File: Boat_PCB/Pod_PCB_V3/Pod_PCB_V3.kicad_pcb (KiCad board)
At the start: 2 copper layers, 48 x 63 mm, 54 parts, among them J1 Tether, J10 Aux, J2 pH SEN0161-V2, J3 TDS SEN0244 via DFR0504, J4 DO SEN0237-A (fit later), J5 Turbidity SEN0189, J6 Pressure SEN0257, J7 DS18B20, J8 Leak probe, J9 Bottom contact, U1 Pololu D36V6F5, U2 AP2112K-3.3, U3 XIAO ESP32-S3, U4 THVD2410, U5 ADS1115

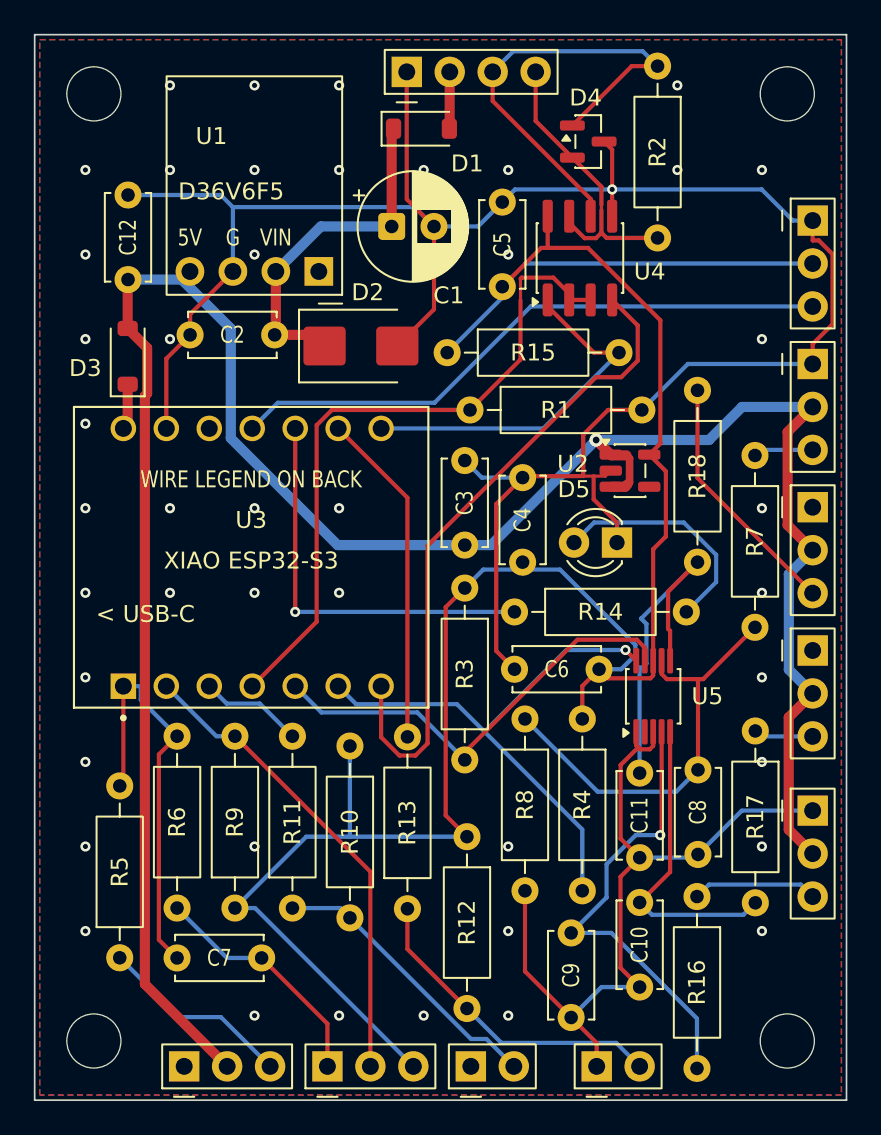
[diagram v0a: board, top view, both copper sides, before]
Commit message: feat(pcb): pod board rev B, reviewed and re-placed on a grid
Pod (Boat_PCB/Pod_PCB_V3), against rev A at 5b3b610. Same 54 footprints,
outline (48 x 63 mm) and netlist; the schematic is untouched.

- Review: every net checks out and every part is needed, so nothing was
  removed. The real faults were decoupling distances: the AP2112's caps
  C3/C4 sat 9.3/9.8 mm from its pins (now 2.2/2.7 mm), C5 was 5.0 mm
  from the THVD2410 (now 2.7) and C6 3.2 mm from the ADS1115 (now 2.3).
- Placement: the right-edge wire-pad groups are on one 8.47 mm pitch and
  the bottom groups on equal 3.4 mm gaps. The twelve upright resistors
  and caps stand in one row on a 3.4 mm pitch; the RX pull-up, DE
  pull-down and LED resistors form a column, and the PRESS/DO series
  resistors sit side by side.
- Back legend on a fixed grid: pad labels level with or centred on their
  pads, group names in one column (right edge) and one row (bottom
  edge), title block centred on the XIAO. Every pad is labelled; rev A
  had no GND label on TDS.
- Re-routed. Track length 1023 -> 949 mm. Vias 50 -> 46: nine GND
  stitching vias dropped and two moved off the legend rows, one TDS_OUT
  via moved 1.2 mm.
- The per-pad solid GND connection moved from C3 to U5 pad 3, the pad
  whose thermal spokes the new routing starves.

ERC 0 -> 0. DRC 0 -> 0. Schematic parity 0 -> 0. Unconnected 0 -> 0.

Docs: CLAUDE.md pod baseline and design brief section 5.

Co-Authored-By: Claude Opus 5.5 <noreply@anthropic.com>
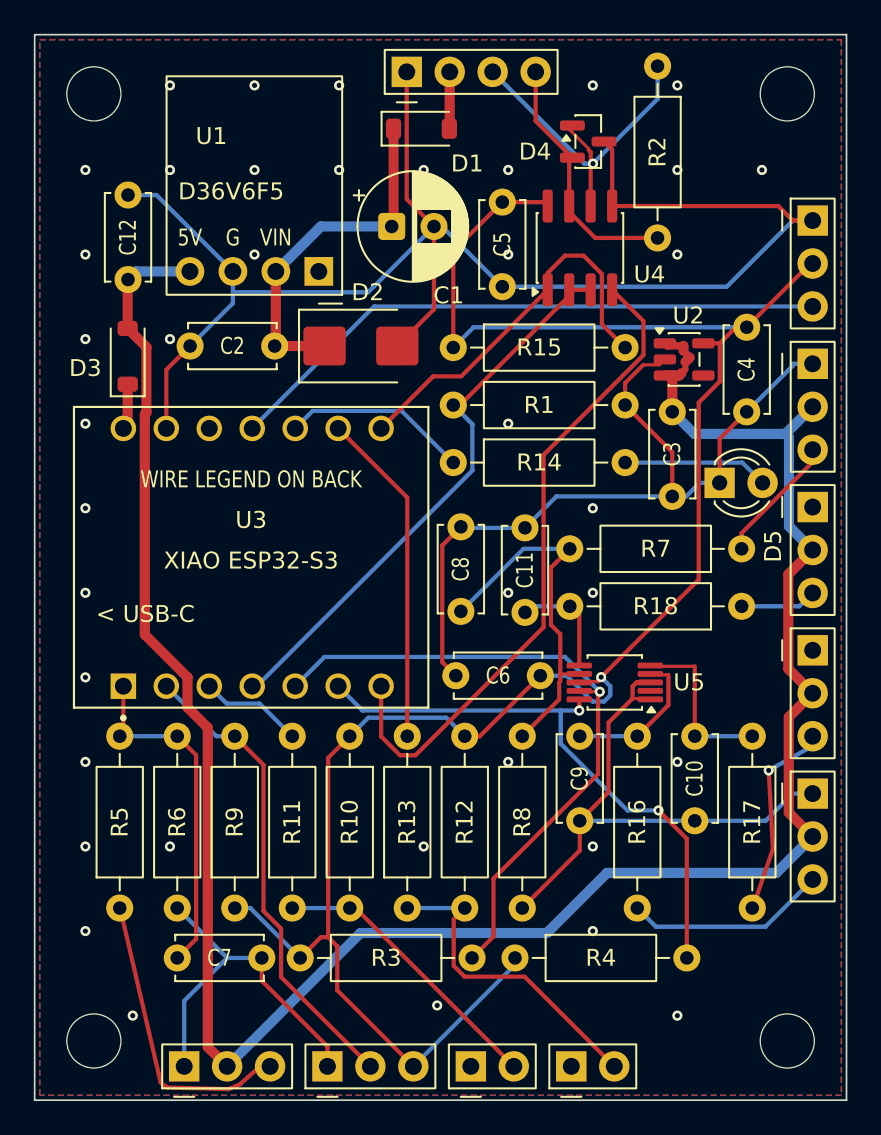
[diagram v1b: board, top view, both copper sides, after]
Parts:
- moved R3 23.9 mm to (115.7, 104.6), turned to 0 degrees
- moved C4 19.2 mm to (142.1, 67.3), turned to -90 degrees
- moved C8 16.9 mm to (125.2, 84.1), turned to 90 degrees
- moved R4 14.7 mm to (128.4, 104.6), turned to 0 degrees
- moved C3 14.6 mm to (137.7, 72.3), turned to -90 degrees
- moved R18 13.0 mm to (141.8, 83.8), turned to 180 degrees
- moved C11 11.7 mm to (129.0, 84.2), turned to 90 degrees
- moved C9 11.6 mm to (132.2, 91.5)
- moved R17 10.5 mm to (142.4, 101.6), turned to 90 degrees
- moved C10 10.4 mm to (139.0, 91.5)
- moved R14 9.54 mm to (124.8, 75.3)
- moved U2 7.32 mm to (138.4, 69.2)
- moved D5 7.02 mm to (140.5, 76.5), turned to 0 degrees
- moved R12 5.94 mm to (125.4, 91.5)
- moved R7 5.58 mm to (141.8, 80.4), turned to 180 degrees
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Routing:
- net /PH_AIN: track 27.4 -> 8.88 mm, vias 1 -> 0
- net /DO_AIN: track 20.8 -> 6.53 mm
- net /I2C_SDA: track 26.7 -> 39.6 mm, vias 0 -> 1
- net /LED_DRV: track 23.8 -> 11.0 mm, vias 1 -> 0
- net +3V3: track 133.8 -> 121.1 mm, vias 0 -> 1
- net /DO_OUT: track 14.8 -> 4.53 mm
- net /TDS_AIN: track 18.3 -> 10.2 mm
- net /TDS_OUT: track 3.52 -> 11.0 mm, vias 0 -> 1
- net /TETHER_A: track 28.0 -> 21.1 mm, vias 0 -> 1
- net /RS485_DE: track 40.4 -> 33.8 mm
- net /LED_A: track 13.8 -> 8.63 mm
- net /TURB_RAW: track 11.5 -> 16.7 mm
- net /PH_OUT: track 7.43 -> 12.0 mm
- net /TURB_ADC: track 24.9 -> 20.5 mm
- net /PRESS_RAW: track 3.55 -> 7.60 mm
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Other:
- board text added: "rev B 2026-09-29"
- board text removed: "rev A 2026-09-26"

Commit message: chore(pcb): V3 carrier and pod order-number markers for PCBWay
Like V3.1, the V3 carrier and the pod will be made by PCBWay, so their
back-silk order-number markers change from JLCPCB's "JLCJLCJLCJLC" to
PCBWay's "WayWayWay" (same spot, size and angle). Pick "Specify a
location" for the product number at checkout. Silkscreen only: the back
silkscreen gerber is the only one that changes on each board. CLAUDE.md
gets a short note on ordering.

Boat_PCB_V3 (rev E): 130.6 x 101.5 mm, 137 footprints, unchanged.
Pod_PCB_V3 (rev B): 48 x 63 mm, 54 footprints, unchanged.
Both: DRC 0 -> 0, unconnected 0 -> 0, schematic parity 0 -> 0, ERC 0 -> 0.
Boat_PCB_V3_1 stays at 0 on all four.

Co-Authored-By: Claude Opus 5.5 <noreply@anthropic.com>
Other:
- board text added: "WayWayWay"
- board text removed: "JLCJLCJLCJLC"
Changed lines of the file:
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@@
 		)
 	)
-	(gr_text "JLCJLCJLCJLC"
+	(gr_text "WayWayWay"
 		(at 112.8635 85.7 0)
 		(layer "B.SilkS")
